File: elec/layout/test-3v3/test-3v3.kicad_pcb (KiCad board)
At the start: 2 copper layers, 8 parts, among them U3 10µH ±20%

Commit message: building successfully
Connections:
- net cathode renamed SW
- C2 pad 2: gnd -> gnd-1
- C3 pad 2: gnd-1 -> gnd
- R1 pad 2: gnd-1 -> gnd
- U1 pad 2: gnd-1 -> gnd
- U2 pad 2: gnd -> gnd-1
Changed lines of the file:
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@@
     (net 0 "")
     (net 1 "hv")
-    (net 2 "gnd")
+    (net 2 "gnd-1")
     (net 3 "hv-1")
-    (net 4 "cathode")
+    (net 4 "SW")
     (net 5 "CB")
-    (net 6 "gnd-1")
+    (net 6 "gnd")
     (net 7 "line")
     (footprint "lib:SOD-323_L1.8-W1.3-LS2.5-RD"
@@
             (layers "F.Cu" "F.Paste" "F.Mask")
             (remove_unused_layers no)
-            (net 6 "gnd-1"))
+            (net 6 "gnd"))
         (pad "1" smd rect
             (at -1.17 0 0)
@@
             (layers "F.Cu" "F.Paste" "F.Mask")
             (remove_unused_layers no)
-            (net 4 "cathode"))
+            (net 4 "SW"))
         (model "${KIPRJMOD}/../../../build/footprints/footprints.3dshapes/SOD-323_L1.7-W1.3-H1.1-LS2.5.step"
             (offset
@@
             (layers "F.Cu" "F.Paste" "F.Mask")
             (remove_unused_layers no)
-            (net 2 "gnd"))
+            (net 2 "gnd-1"))
         (pad "1" smd rect
             (at -1 0 0)
@@
             (layers "F.Cu" "F.Paste" "F.Mask")
             (remove_unused_layers no)
-            (net 4 "cathode"))
+            (net 4 "SW"))
         (pad "1" smd rect
             (at -0.55 0 0)
@@
             (layers "F.Cu" "F.Paste" "F.Mask")
             (remove_unused_layers no)
-            (net 4 "cathode"))
+            (net 4 "SW"))
         (model "${KIPRJMOD}/../../../build/footprints/footprints.3dshapes/IND-SMD_L4.0-W4.0-H1.9.step"
             (offset
@@
             (layers "F.Cu" "F.Paste" "F.Mask")
             (remove_unused_layers no)
-            (net 2 "gnd"))
+            (net 2 "gnd-1"))
         (pad "1" smd rect
             (at 1.35 0.95 0)
@@
             (layers "F.Cu" "F.Paste" "F.Mask")
             (remove_unused_layers no)
-            (net 4 "cathode"))
+            (net 4 "SW"))
         (pad "5" smd rect
             (at -1.35 0 0)
@@
             (layers "F.Cu" "F.Paste" "F.Mask")
             (remove_unused_layers no)
-            (net 6 "gnd-1"))
+            (net 6 "gnd"))
         (pad "1" smd rect
             (at -1 0 0)
@@
             (layers "F.Cu" "F.Paste" "F.Mask")
             (remove_unused_layers no)
-            (net 6 "gnd-1"))
+            (net 6 "gnd"))
         (pad "1" smd rect
             (at -0.43 0 0)

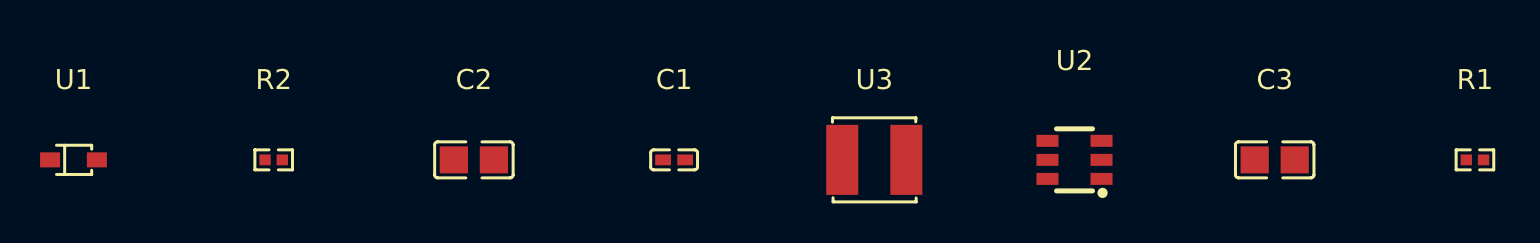
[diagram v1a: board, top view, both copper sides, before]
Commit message: Update layouts to kicad 9, add default build for layout reuse
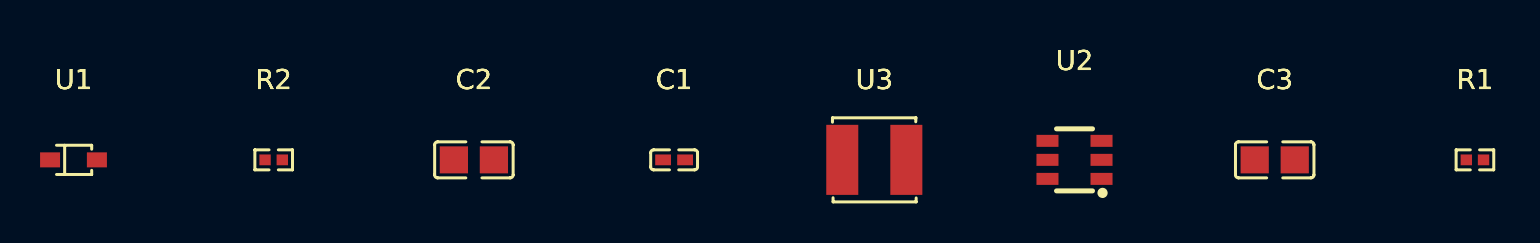
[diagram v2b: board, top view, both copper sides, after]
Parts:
- C2: value 10µF ±10% 25V X5R -> 4.7µF ±10% 25V X5R
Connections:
- net SW renamed cathode
- net line renamed FB
- C2 pad 1: hv -> hv-1
- C3 pad 1: hv-1 -> hv
- R2 pad 1: hv-1 -> hv
- U2 pad 4: hv -> hv-1
- U2 pad 5: hv -> hv-1
- U3 pad 2: hv-1 -> hv
